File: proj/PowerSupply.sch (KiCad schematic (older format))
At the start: 0 parts

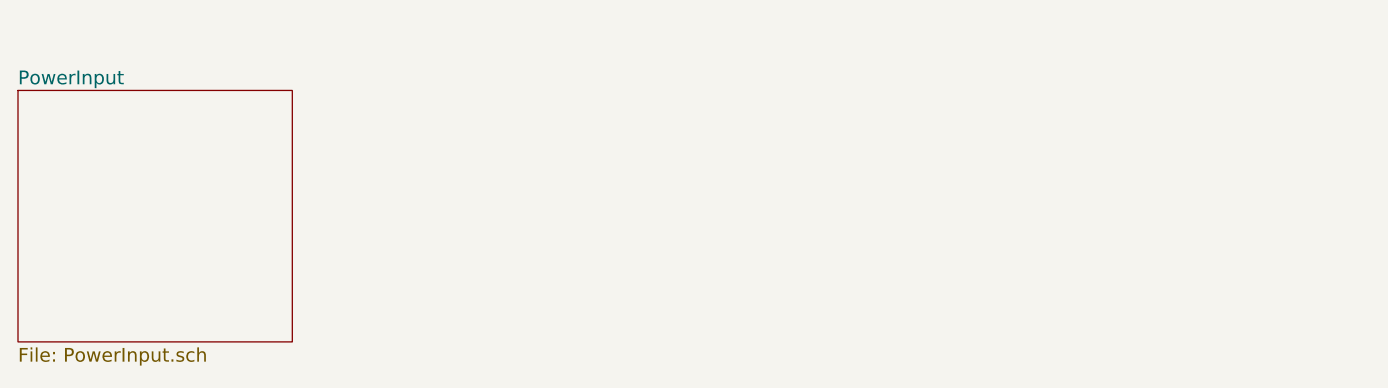
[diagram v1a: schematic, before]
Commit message: Add DC-DC
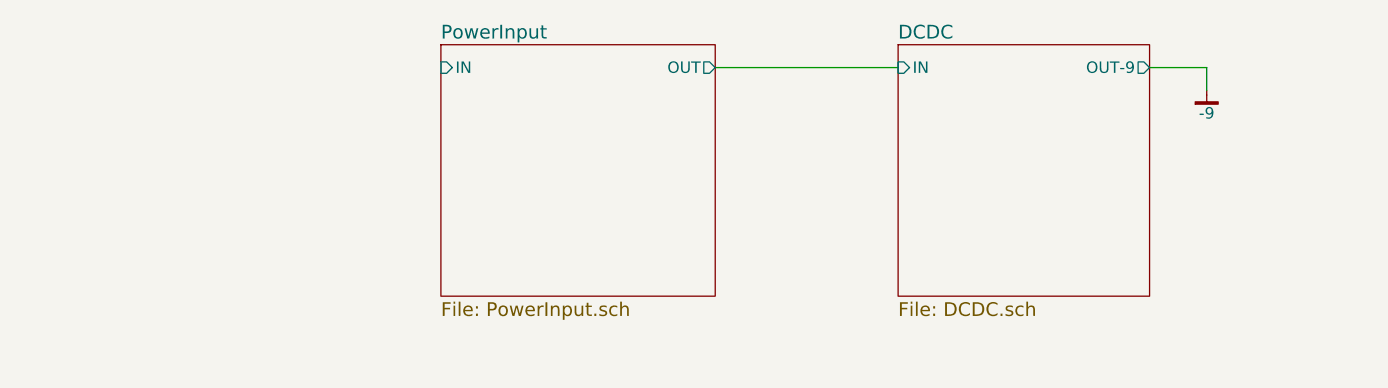
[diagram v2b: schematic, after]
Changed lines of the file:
@@
 $Descr USLegal 14000 8500
 encoding utf-8
-Sheet 2 13
+Sheet 2 14
 Title "Power Supply Block Diagram"
 Date "2015-02-28"
@@
 $EndDescr
 $Sheet
-S 2100 2200 1200 1100
+S 3950 2000 1200 1100
 U 54F49966
 F0 "PowerInput" 60
 F1 "PowerInput.sch" 60
+F2 "OUT" O R 5150 2100 50
+F3 "IN" I L 3950 2100 50
 $EndSheet
+$Sheet
+S 5950 2000 1100 1100
+U 54F4F7B6
+F0 "DCDC" 60
+F1 "DCDC.sch" 60
+F2 "OUT-9" O R 7050 2100 50
+F3 "IN" I L 5950 2100 50
+$EndSheet
+$Comp
+L -9 #PWR1
+U 1 1 54F50E66
+P 7300 2200
+F 0 "#PWR1" H 7300 2150 30  0001 C CNN
+F 1 "-9" H 7300 2100 50  0000 C CNN
+F 2 "" H 7300 2200 60  0000 C CNN
+F 3 "" H 7300 2200 60  0000 C CNN
+	1    7300 2200
+	1    0    0    -1
+$EndComp
+Wire Wire Line
+	7300 2200 7300 2100
+Wire Wire Line
+	7300 2100 7050 2100
+Wire Wire Line
+	5150 2100 5950 2100
 $EndSCHEMATC

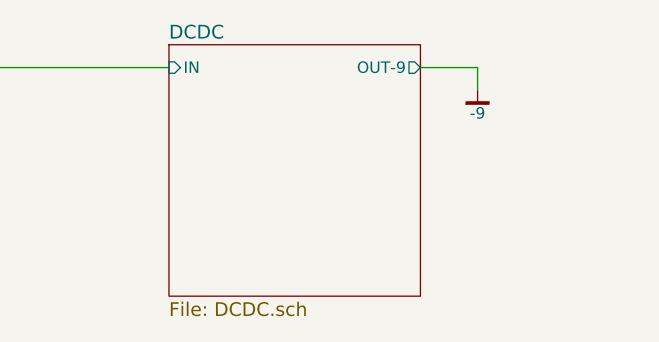
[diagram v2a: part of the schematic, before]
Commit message: Finish USB subcircuit
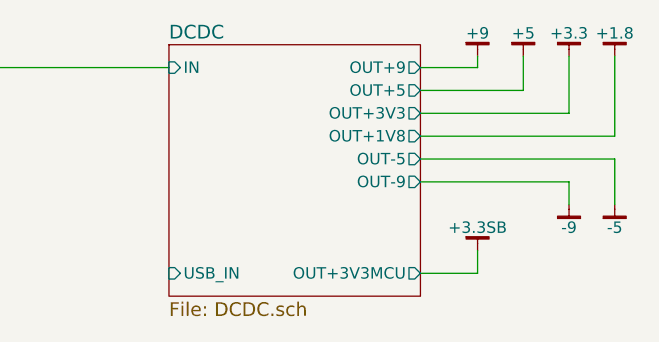
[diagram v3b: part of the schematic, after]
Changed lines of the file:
@@
 F0 "DCDC" 60
 F1 "DCDC.sch" 60
-F2 "OUT-9" O R 7050 2100 50
+F2 "OUT-9" O R 7050 2600 50
 F3 "IN" I L 5950 2100 50
+F4 "OUT+3V3" O R 7050 2300 50
+F5 "OUT+9" O R 7050 2100 50
+F6 "OUT+5" O R 7050 2200 50
+F7 "OUT-5" O R 7050 2500 50
+F8 "OUT+1V8" O R 7050 2400 50
+F9 "USB_IN" I L 5950 3000 50
+F10 "OUT+3V3MCU" O R 7050 3000 50
 $EndSheet
+Wire Wire Line
+	5150 2100 5950 2100
 $Comp
-L -9 #PWR1
-U 1 1 54F50E66
-P 7300 2200
-F 0 "#PWR1" H 7300 2150 30  0001 C CNN
-F 1 "-9" H 7300 2100 50  0000 C CNN
-F 2 "" H 7300 2200 60  0000 C CNN
-F 3 "" H 7300 2200 60  0000 C CNN
-	1    7300 2200
+L +9 #PWR?
+U 1 1 54F67632
+P 7300 2050
+F 0 "#PWR?" H 7300 2100 30  0001 C CNN
+F 1 "+9" H 7300 2150 50  0000 C CNN
+F 2 "" H 7300 2050 60  0000 C CNN
+F 3 "" H 7300 2050 60  0000 C CNN
+	1    7300 2050
 	1    0    0    -1
 $EndComp
 Wire Wire Line
-	7300 2200 7300 2100
+	7050 2100 7300 2100
 Wire Wire Line
-	7300 2100 7050 2100
+	7300 2100 7300 2050
+$Comp
+L +5 #PWR?
+U 1 1 54F676AE
+P 7500 2050
+F 0 "#PWR?" H 7500 2100 30  0001 C CNN
+F 1 "+5" H 7500 2150 50  0000 C CNN
+F 2 "" H 7500 2050 60  0000 C CNN
+F 3 "" H 7500 2050 60  0000 C CNN
+	1    7500 2050
+	1    0    0    -1
+$EndComp
 Wire Wire Line
-	5150 2100 5950 2100
+	7500 2050 7500 2200
+Wire Wire Line
+	7500 2200 7050 2200
+$Comp
+L +3.3 #PWR?
+U 1 1 54F67709
+P 7700 2050
+F 0 "#PWR?" H 7700 2100 30  0001 C CNN
+F 1 "+3.3" H 7700 2150 50  0000 C CNN
+F 2 "" H 7700 2050 60  0000 C CNN
+F 3 "" H 7700 2050 60  0000 C CNN
+	1    7700 2050
+	1    0    0    -1
+$EndComp
+Wire Wire Line
+	7700 2050 7700 2300
+Wire Wire Line
+	7700 2300 7050 2300
+$Comp
+L +1.8 #PWR?
+U 1 1 54F67766
+P 7900 2050
+F 0 "#PWR?" H 7900 2100 30  0001 C CNN
+F 1 "+1.8" H 7900 2150 50  0000 C CNN
+F 2 "" H 7900 2050 60  0000 C CNN
+F 3 "" H 7900 2050 60  0000 C CNN
+	1    7900 2050
+	1    0    0    -1
+$EndComp
+Wire Wire Line
+	7900 2050 7900 2400
+Wire Wire Line
+	7900 2400 7050 2400
+$Comp
+L -5 #PWR?
+U 1 1 54F679B4
+P 7900 2700
+F 0 "#PWR?" H 7900 2650 30  0001 C CNN
+F 1 "-5" H 7900 2600 50  0000 C CNN
+F 2 "" H 7900 2700 60  0000 C CNN
+F 3 "" H 7900 2700 60  0000 C CNN
+	1    7900 2700
+	1    0    0    -1
+$EndComp
+Wire Wire Line
+	7900 2700 7900 2500
+Wire Wire Line
+	7900 2500 7050 2500
+$Comp
+L -9 #PWR?
+U 1 1 54F67A8D
+P 7700 2700
+F 0 "#PWR?" H 7700 2650 30  0001 C CNN
+F 1 "-9" H 7700 2600 50  0000 C CNN
+F 2 "" H 7700 2700 60  0000 C CNN
+F 3 "" H 7700 2700 60  0000 C CNN
+	1    7700 2700
+	1    0    0    -1
+$EndComp
+Wire Wire Line
+	7700 2700 7700 2600
+Wire Wire Line
+	7700 2600 7050 2600
+$Comp
+L +3.3SB #PWR?
+U 1 1 54F67AF0
+P 7300 2900
+F 0 "#PWR?" H 7300 2950 30  0001 C CNN
+F 1 "+3.3SB" H 7300 3000 50  0000 C CNN
+F 2 "" H 7300 2900 60  0000 C CNN
+F 3 "" H 7300 2900 60  0000 C CNN
+	1    7300 2900
+	1    0    0    -1
+$EndComp
+Wire Wire Line
+	7300 2900 7300 3000
+Wire Wire Line
+	7300 3000 7050 3000
 $EndSCHEMATC
